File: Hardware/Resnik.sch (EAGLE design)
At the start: 179 parts, among them IC1 ATMEGA644M, J1 CONN_82.54_SCREW, J3 CONN_42.54_SCREW, J4 CONN_82.54_SCREW, Q1 DMG3404, Q2 DMG3404, Q3 FDN360P, Q4 FDN360P, Q5 FDN360P, Q6 DMG3404, U1 TLV61220DBV, U10 TPS22917DBV, U11 SN74AUP1G04YFP, U12 SN74AUP1G04YFP, U13 SN74AUP2G86SOT833-1, U14 SN74AUP2G08DQE, U15 SN74AUP2G08DQE, U16 SN74AUP2G08DQE, U17 MIC2039MT, U18 MIC2039MT, U19 MIC2039MT, U2 TPS62822DLC, U20 MIC2039MT, U21 TPS22917DBV, U22 TPS22917DBV, U23 FT231X-Q, U24 SN74LVC1G3157DRL, U25 SN74AUP3G34DCU, U26 TXS0102DQM, U27 TXS0108RGY, U28 TXS0108RGY, U29 TXS0104RGY, U3 TPS61032RSA, U30 MCP4726A2SOT-23, U31 BME280, U32 ADS1115, U33 ADS1115, U34 INA211DCK, U35 INA210DCK, U36 TCA9555RTW, U5 BQ2980RUG, U6 TPS2105, U7 LTC4412S6, U8 TPL5111DDC, U9 TPS79733

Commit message: Updated inductor L2 layout
Fixed size and part number of inductor to match XHMI layout
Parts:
- L2: DIGIKEY 732-1208-1-ND -> 732-10707-1-ND; MPN 74477110 -> 74439346100
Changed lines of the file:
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@@
 <setting verticaltext="up"/>
 </settings>
-<grid distance="0.1" unitdist="inch" unit="inch" style="lines" multiple="1" display="no" altdistance="0.01" altunitdist="inch" altunit="mm"/>
+<grid distance="0.1" unitdist="inch" unit="inch" style="lines" multiple="1" display="no" altdistance="0.01" altunitdist="inch" altunit="inch"/>
 <layers>
-<layer number="1" name="Top" color="4" fill="1" visible="yes" active="no"/>
-<layer number="2" name="Route2" color="16" fill="1" visible="yes" active="no"/>
-<layer number="3" name="Route3" color="17" fill="1" visible="yes" active="no"/>
-<layer number="4" name="Route4" color="18" fill="1" visible="yes" active="no"/>
-<layer number="5" name="Route5" color="19" fill="1" visible="yes" active="no"/>
-<layer number="6" name="Route6" color="25" fill="1" visible="yes" active="no"/>
-<layer number="7" name="Route7" color="26" fill="1" visible="yes" active="no"/>
-<layer number="8" name="Route8" color="27" fill="1" visible="yes" active="no"/>
-<layer number="9" name="Route9" color="28" fill="1" visible="yes" active="no"/>
-<layer number="10" name="Route10" color="29" fill="1" visible="yes" active="no"/>
-<layer number="11" name="Route11" color="30" fill="1" visible="yes" active="no"/>
-<layer number="12" name="Route12" color="20" fill="1" visible="yes" active="no"/>
-<layer number="13" name="Route13" color="21" fill="1" visible="yes" active="no"/>
-<layer number="14" name="Route14" color="22" fill="1" visible="yes" active="no"/>
-<layer number="15" name="Route15" color="23" fill="1" visible="yes" active="no"/>
-<layer number="16" name="Bottom" color="1" fill="1" visible="yes" active="no"/>
-<layer number="17" name="Pads" color="2" fill="1" visible="yes" active="no"/>
-<layer number="18" name="Vias" color="2" fill="1" visible="yes" active="no"/>
-<layer number="19" name="Unrouted" color="6" fill="1" visible="yes" active="no"/>
-<layer number="20" name="Dimension" color="24" fill="1" visible="yes" active="no"/>
-<layer number="21" name="tPlace" color="7" fill="1" visible="yes" active="no"/>
-<layer number="22" name="bPlace" color="7" fill="1" visible="yes" active="no"/>
-<layer number="23" name="tOrigins" color="15" fill="1" visible="yes" active="no"/>
-<layer number="24" name="bOrigins" color="15" fill="1" visible="yes" active="no"/>
-<layer number="25" name="tNames" color="7" fill="1" visible="yes" active="no"/>
-<layer number="26" name="bNames" color="7" fill="1" visible="yes" active="no"/>
-<layer number="27" name="tValues" color="7" fill="1" visible="yes" active="no"/>
-<layer number="28" name="bValues" color="7" fill="1" visible="yes" active="no"/>
+<layer number="1" name="Top" color="4" fill="1" visible="no" active="no"/>
+<layer number="2" name="Route2" color="16" fill="1" visible="no" active="no"/>
+<layer number="3" name="Route3" color="17" fill="1" visible="no" active="no"/>
+<layer number="4" name="Route4" color="18" fill="1" visible="no" active="no"/>
+<layer number="5" name="Route5" color="19" fill="1" visible="no" active="no"/>
+<layer number="6" name="Route6" color="25" fill="1" visible="no" active="no"/>
+<layer number="7" name="Route7" color="26" fill="1" visible="no" active="no"/>
+<layer number="8" name="Route8" color="27" fill="1" visible="no" active="no"/>
+<layer number="9" name="Route9" color="28" fill="1" visible="no" active="no"/>
+<layer number="10" name="Route10" color="29" fill="1" visible="no" active="no"/>
+<layer number="11" name="Route11" color="30" fill="1" visible="no" active="no"/>
+<layer number="12" name="Route12" color="20" fill="1" visible="no" active="no"/>
+<layer number="13" name="Route13" color="21" fill="1" visible="no" active="no"/>
+<layer number="14" name="Route14" color="22" fill="1" visible="no" active="no"/>
+<layer number="15" name="Route15" color="23" fill="1" visible="no" active="no"/>
+<layer number="16" name="Bottom" color="1" fill="1" visible="no" active="no"/>
+<layer number="17" name="Pads" color="2" fill="1" visible="no" active="no"/>
+<layer number="18" name="Vias" color="2" fill="1" visible="no" active="no"/>
+<layer number="19" name="Unrouted" color="6" fill="1" visible="no" active="no"/>
+<layer number="20" name="Dimension" color="24" fill="1" visible="no" active="no"/>
+<layer number="21" name="tPlace" color="7" fill="1" visible="no" active="no"/>
+<layer number="22" name="bPlace" color="7" fill="1" visible="no" active="no"/>
+<layer number="23" name="tOrigins" color="15" fill="1" visible="no" active="no"/>
+<layer number="24" name="bOrigins" color="15" fill="1" visible="no" active="no"/>
+<layer number="25" name="tNames" color="7" fill="1" visible="no" active="no"/>
+<layer number="26" name="bNames" color="7" fill="1" visible="no" active="no"/>
+<layer number="27" name="tValues" color="7" fill="1" visible="no" active="no"/>
+<layer number="28" name="bValues" color="7" fill="1" visible="no" active="no"/>
 <layer number="29" name="tStop" color="7" fill="3" visible="no" active="no"/>
 <layer number="30" name="bStop" color="7" fill="6" visible="no" active="no"/>
@@
 <layer number="35" name="tGlue" color="7" fill="4" visible="no" active="no"/>
 <layer number="36" name="bGlue" color="7" fill="5" visible="no" active="no"/>
-<layer number="37" name="tTest" color="7" fill="1" visible="yes" active="no"/>
-<layer number="38" name="bTest" color="7" fill="1" visible="yes" active="no"/>
+<layer number="37" name="tTest" color="7" fill="1" visible="no" active="no"/>
+<layer number="38" name="bTest" color="7" fill="1" visible="no" active="no"/>
 <layer number="39" name="tKeepout" color="4" fill="11" visible="no" active="no"/>
 <layer number="40" name="bKeepout" color="1" fill="11" visible="no" active="no"/>
@@
 <layer number="44" name="Drills" color="7" fill="1" visible="no" active="no"/>
 <layer number="45" name="Holes" color="7" fill="1" visible="no" active="no"/>
-<layer number="46" name="Milling" color="3" fill="1" visible="yes" active="no"/>
-<layer number="47" name="Measures" color="7" fill="1" visible="yes" active="no"/>
-<layer number="48" name="Document" color="7" fill="1" visible="yes" active="no"/>
-<layer number="49" name="Reference" color="7" fill="1" visible="yes" active="no"/>
-<layer number="50" name="dxf" color="7" fill="1" visible="yes" active="no"/>
-<layer number="51" name="tDocu" color="7" fill="1" visible="yes" active="no"/>
-<layer number="52" name="bDocu" color="7" fill="1" visible="yes" active="no"/>
-<layer number="53" name="tGND_GNDA" color="7" fill="1" visible="yes" active="no"/>
-<layer number="54" name="bGND_GNDA" color="7" fill="1" visible="yes" active="no"/>
-<layer number="56" name="wert" color="7" fill="1" visible="yes" active="no"/>
-<layer number="57" name="tCAD" color="7" fill="1" visible="yes" active="no"/>
-<layer number="59" name="tCarbon" color="7" fill="1" visible="yes" active="no"/>
-<layer number="60" name="bCarbon" color="7" fill="1" visible="yes" active="no"/>
+<layer number="46" name="Milling" color="3" fill="1" visible="no" active="no"/>
+<layer number="47" name="Measures" color="7" fill="1" visible="no" active="no"/>
+<layer number="48" name="Document" color="7" fill="1" visible="no" active="no"/>
+<layer number="49" name="Reference" color="7" fill="1" visible="no" active="no"/>
+<layer number="50" name="dxf" color="7" fill="1" visible="no" active="no"/>
+<layer number="51" name="tDocu" color="7" fill="1" visible="no" active="no"/>
+<layer number="52" name="bDocu" color="7" fill="1" visible="no" active="no"/>
+<layer number="53" name="tGND_GNDA" color="7" fill="1" visible="no" active="no"/>
+<layer number="54" name="bGND_GNDA" color="7" fill="1" visible="no" active="no"/>
+<layer number="56" name="wert" color="7" fill="1" visible="no" active="no"/>
+<layer number="57" name="tCAD" color="7" fill="1" visible="no" active="no"/>
+<layer number="59" name="tCarbon" color="7" fill="1" visible="no" active="no"/>
+<layer number="60" name="bCarbon" color="7" fill="1" visible="no" active="no"/>
 <layer number="88" name="SimResults" color="9" fill="1" visible="yes" active="yes"/>
 <layer number="89" name="SimProbes" color="9" fill="1" visible="yes" active="yes"/>
@@
 <part name="U3" library="bschulz" deviceset="TPS6103*" device="RSA" technology="2" value="TPS61032RSA"/>
 <part name="L2" library="bschulz" deviceset="INDUCTOR" device="XHMI_6.65X6.45" value="10uH">
-<attribute name="DIGIKEY" value="732-1208-1-ND"/>
+<attribute name="DIGIKEY" value="732-10707-1-ND"/>
 <attribute name="MF" value="Wurth"/>
-<attribute name="MPN" value="74477110"/>
+<attribute name="MPN" value="74439346100"/>
 </part>
 <part name="C2" library="bschulz_passives" deviceset="C-EU" device="C0805" technology="22UF" value="22uF"/>

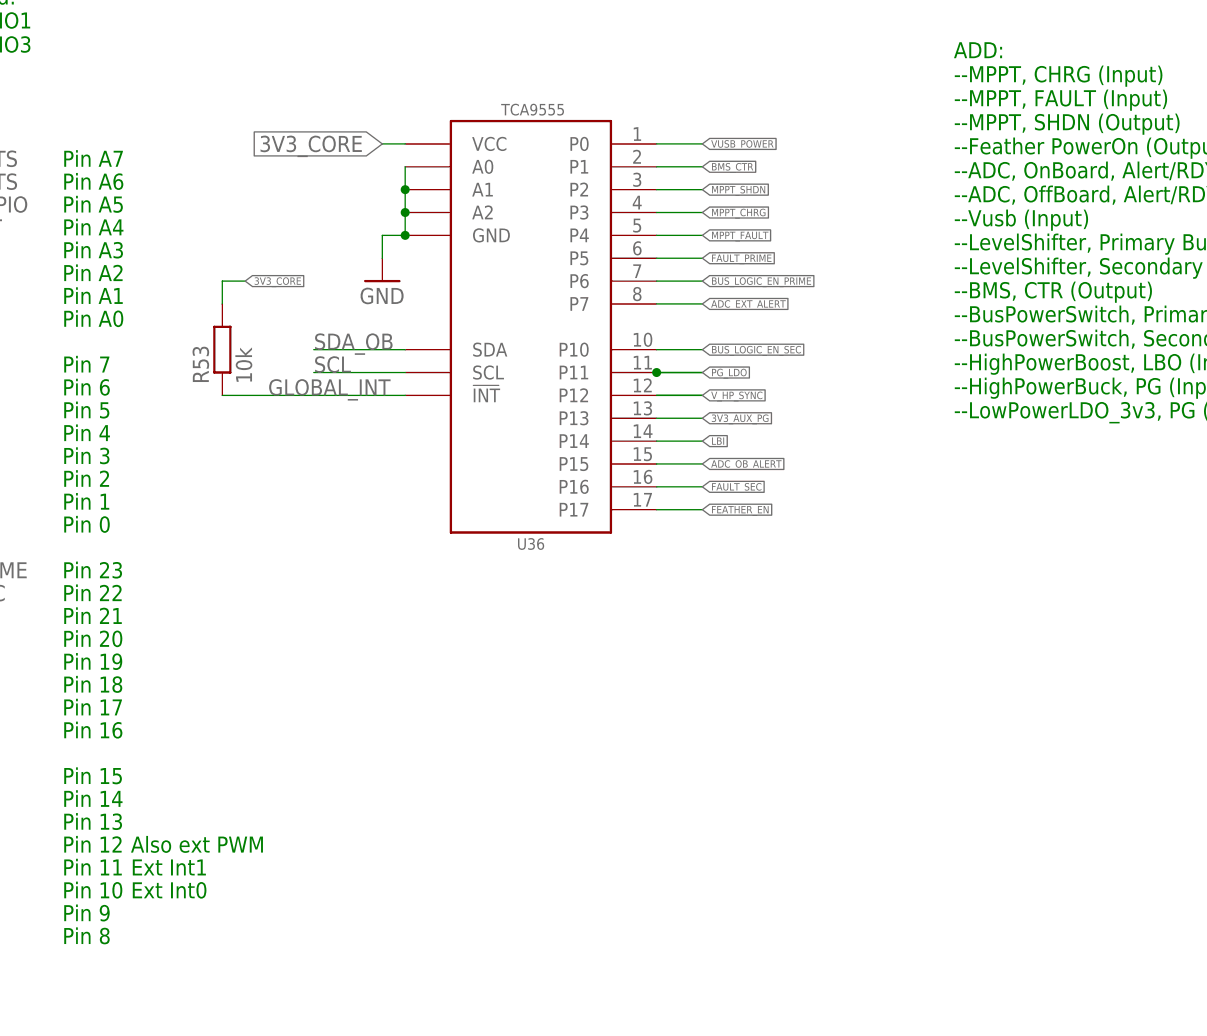
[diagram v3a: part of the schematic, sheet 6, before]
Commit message: First round of fixes to hardware
changed SD card holder, power switches, power switch topology, add pull up resistors to IO expander, to allow for new non-internal pull up module, added some silkscreen, added 3v3 core I2C pullups
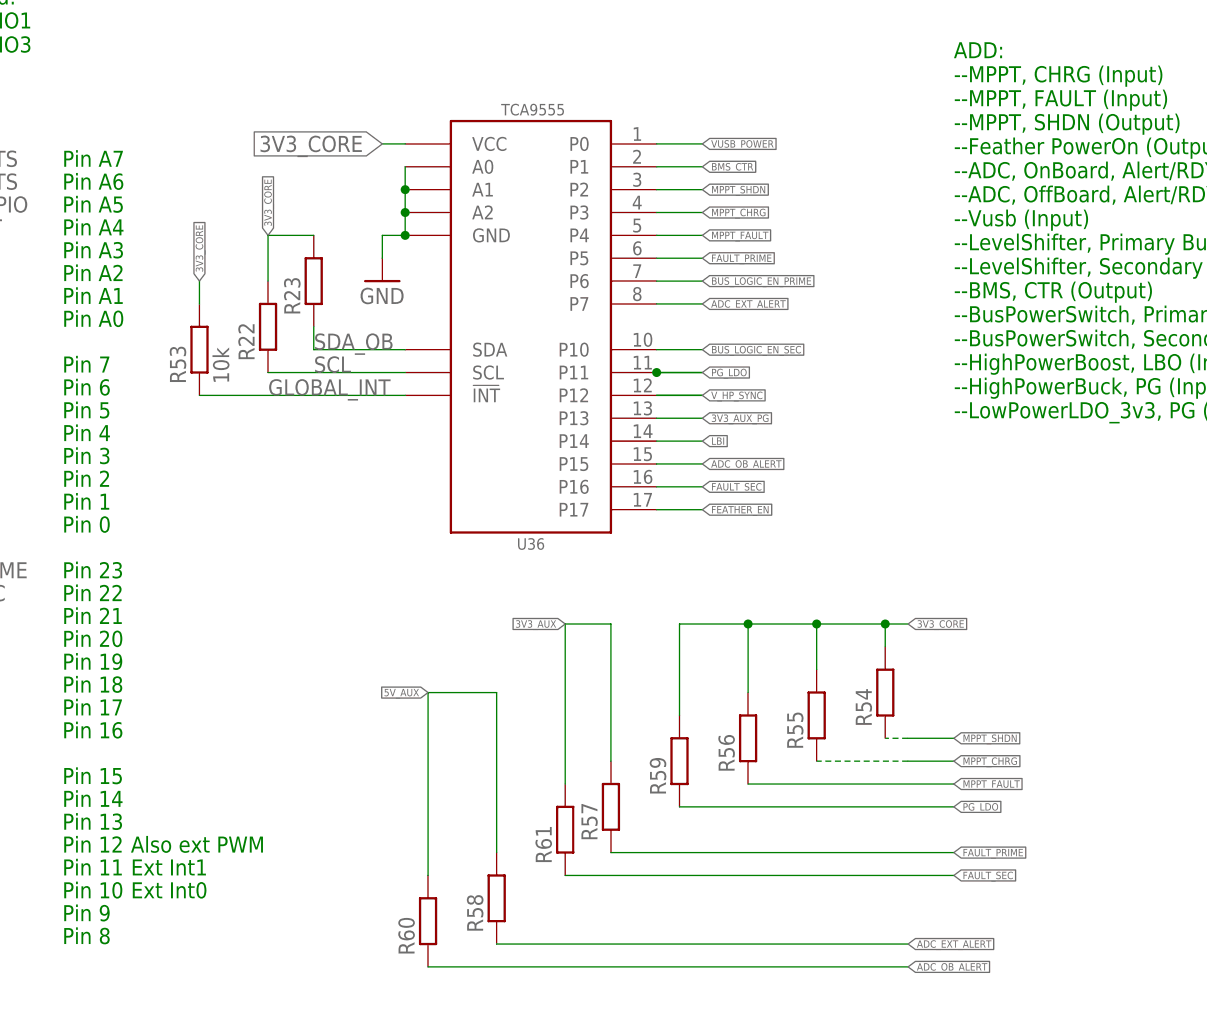
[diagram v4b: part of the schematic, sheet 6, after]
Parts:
- added R54, R55, R56, R57, R58, R59, R60, R61: (no value), bschulz_passives:R-EU_R0402
- R22, R23: value 10k -> (none); device bschulz_passives:R-EU_10KR0402 -> bschulz_passives:R-EU_R0402
- SD1: value MICROSD -> MICROSDCD; device bschulz:MICROSD -> bschulz:MICROSDCD
- U17, U18, U19, U20: value MIC2039MT -> MIC2544MSOP; device bschulz:MIC2039MT -> bschulz:MIC2544MSOP
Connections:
- net 3V3_AUX: now also R57.2, R61.2, U18.IN, U20.IN; no longer U18.VIN, U20.VIN
- net 3V3_CORE: now also R22.2, R23.2, R54.2, R55.2, R56.2, R59.2
- net 5V_AUX: now also R58.2, R60.2, U17.IN, U19.IN; no longer U17.VIN, U19.VIN
- net ADC_EXT_ALERT: now also R58.1
- net ADC_OB_ALERT: now also R60.1
- net FAULT_PRIME: now also R57.1, U19.!FLG, U20.!FLG; no longer U19.!FAULT, U20.!FAULT
- net FAULT_SEC: now also R61.1, U17.!FLG, U18.!FLG; no longer U17.!FAULT, U18.!FAULT
- net GND: now also S1.S, S2.S; no longer R22.1, R23.1
- net MPPT_CHRG: now also R55.1
- net MPPT_FAULT: now also R56.1
- net MPPT_SHDN: now also R54.1
- net N$27: now also U19.ILIM; no longer U19.ILIMIT
- net N$28: no longer R23.2
- net N$33: now also U20.ILIM; no longer U20.ILIMIT
- net N$35: no longer R22.2
- net N$38: now also U17.ILIM; no longer U17.ILIMIT
- net N$41: now also U18.ILIM; no longer U18.ILIMIT
- net PG_LDO: now also R59.1
- net SCL: now also R22.1
- net SDA_OB: now also R23.1
- net VBUS_PRIME: now also U19.OUT, U20.OUT; no longer U19.VOUT, U20.VOUT
- net VBUS_SEC: now also U17.OUT, U18.OUT; no longer U17.VOUT, U18.VOUT
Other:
- moved on the sheet: R53

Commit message: Added dimensions, updated part numbers
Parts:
- R26, R27, R28, R29: device bschulz_passives:R-EU_287R0402 -> bschulz_passives:R-EU_232R0402
- R30, R31, R32, R33: device bschulz_passives:R-EU_287R0402 -> bschulz_passives:R-EU_453R0402

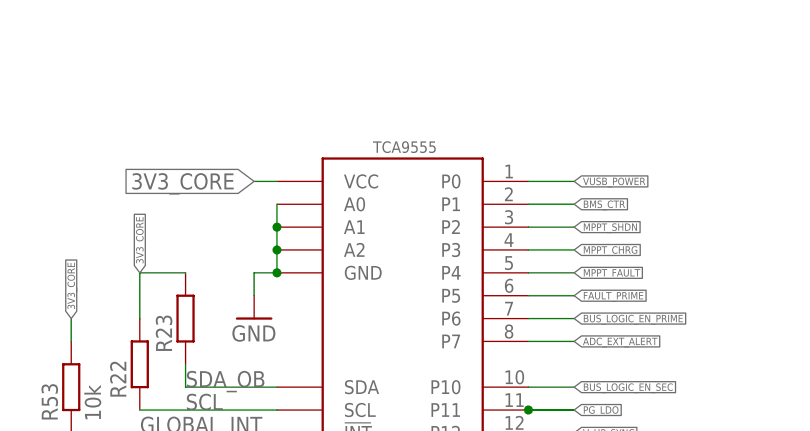
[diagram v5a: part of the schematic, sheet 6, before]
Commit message: Fixed part value for TCA9555 (to TCA9535)
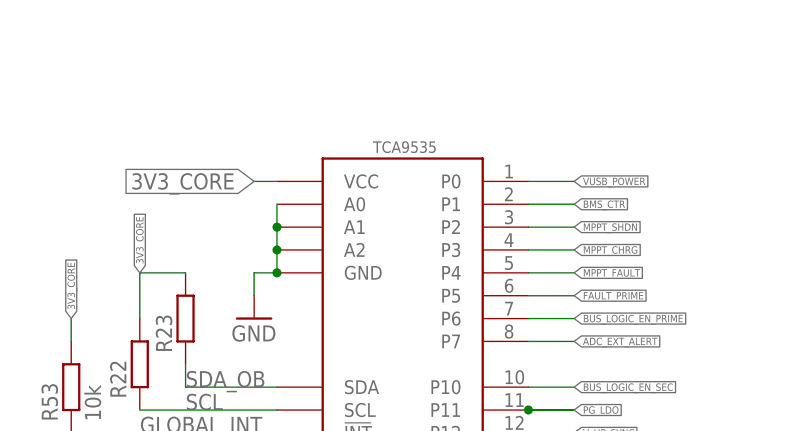
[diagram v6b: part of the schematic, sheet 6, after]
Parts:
- U36: value TCA9555RTW -> TCA9535RTW; device bschulz:TCA9555RTW -> bschulz:TCA9535RTW
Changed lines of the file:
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@@
 <part name="J8" library="bschulz" deviceset="JST_2MM_MALE" device=""/>
 <part name="F1" library="bschulz" deviceset="PPTC" device="1.5A"/>
-<part name="U36" library="bschulz" deviceset="TCA9555" device="RTW"/>
+<part name="U36" library="bschulz" deviceset="TCA95*5" device="RTW" technology="3" value="TCA9535RTW"/>
 <part name="GND70" library="supply1" library_urn="urn:adsk.eagle:library:371" deviceset="GND" device=""/>
 <part name="C28" library="bschulz_passives" deviceset="C-EU" device="C0402" technology="0.1UF" value="0.1uF"/>
@@
 </instance>
 <instance part="U36" gate="G$1" x="167.64" y="86.36" smashed="yes">
+<attribute name="DISP" x="169.164" y="110.49" size="1.27" layer="95" ratio="15" align="center"/>
 <attribute name="NAME" x="168.91" y="62.23" size="1.27" layer="95" ratio="15" align="center"/>
 </instance>

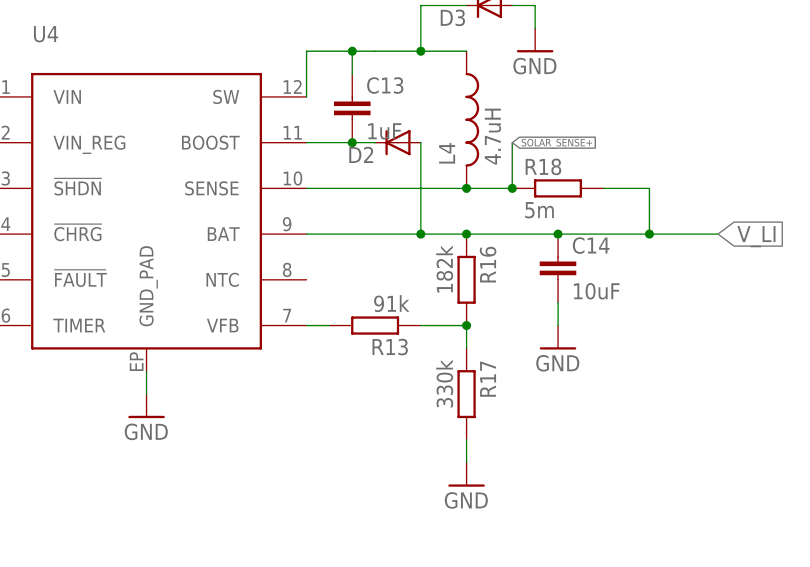
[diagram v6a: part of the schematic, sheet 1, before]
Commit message: Fixed MPPT set resistors
Fixed the order of the MPPT voltage set resistors. Correct values were used, but in the wrong orientation, this has been corrected
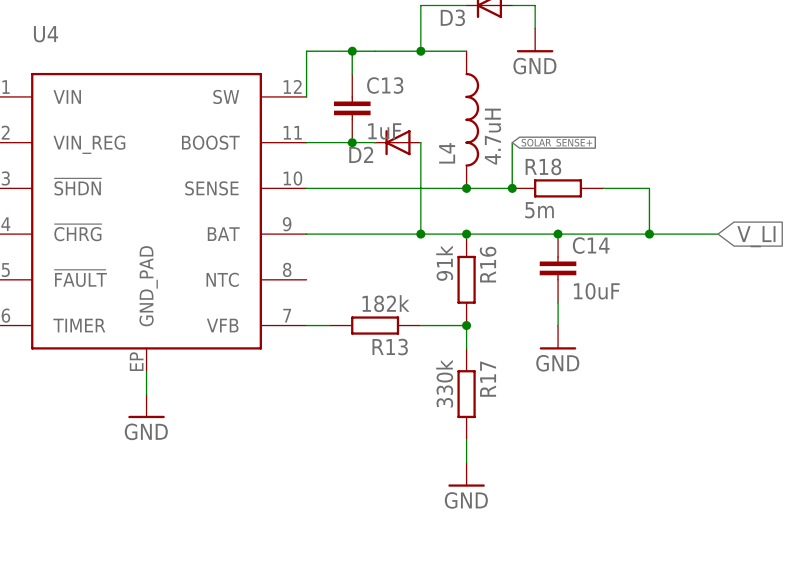
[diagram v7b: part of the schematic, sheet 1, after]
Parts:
- R13: value 91k -> 182k; device bschulz_passives:R-EU_91KR0603 -> bschulz_passives:R-EU_182KR0603
- R16: value 182k -> 91k; device bschulz_passives:R-EU_182KR0603 -> bschulz_passives:R-EU_91KR0603
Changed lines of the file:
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@@
 <part name="GND16" library="supply1" library_urn="urn:adsk.eagle:library:371" deviceset="GND" device=""/>
 <part name="GND18" library="supply1" library_urn="urn:adsk.eagle:library:371" deviceset="GND" device=""/>
-<part name="R13" library="bschulz_passives" deviceset="R-EU_" device="R0603" technology="91K" value="91k"/>
-<part name="R16" library="bschulz_passives" deviceset="R-EU_" device="R0603" technology="182K" value="182k"/>
+<part name="R13" library="bschulz_passives" deviceset="R-EU_" device="R0603" technology="182K" value="182k"/>
+<part name="R16" library="bschulz_passives" deviceset="R-EU_" device="R0603" technology="91K" value="91k"/>
 <part name="R17" library="bschulz_passives" deviceset="R-EU_" device="R0603" technology="330K" value="330k"/>
 <part name="GND20" library="supply1" library_urn="urn:adsk.eagle:library:371" deviceset="GND" device=""/>
